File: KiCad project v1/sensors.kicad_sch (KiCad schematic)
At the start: 15 parts, among them Q1 TEMT6000X01, U6 BME280, U7 MAX4466EXK

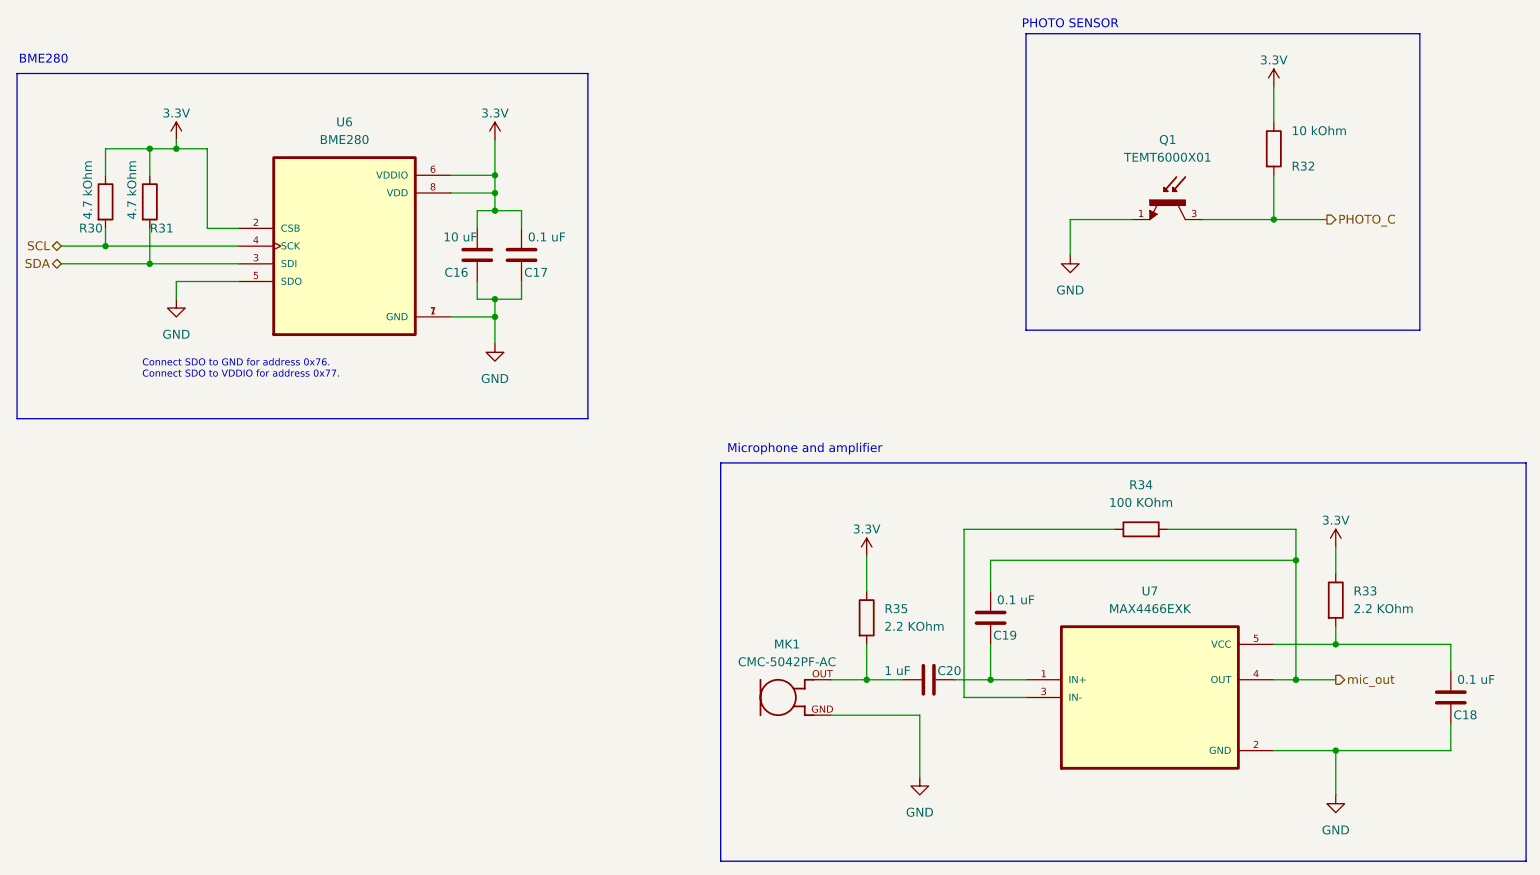
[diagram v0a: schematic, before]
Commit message: Added an OLED I2C display connector, boot and reset buttons, and breakout for remaining pins.
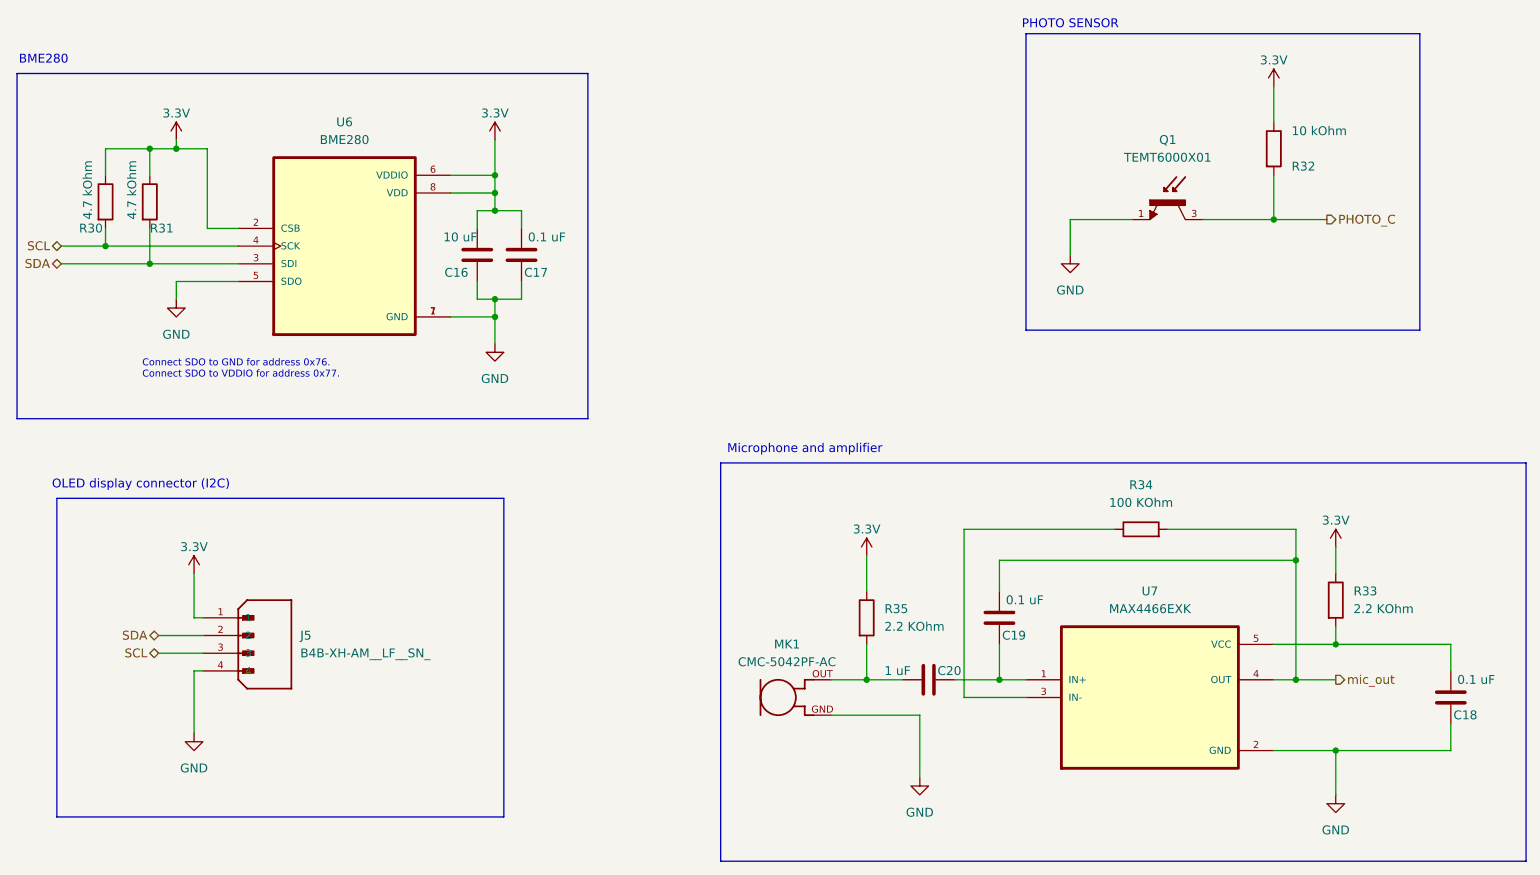
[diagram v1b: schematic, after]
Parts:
- added J5: B4B-XH-AM__LF__SN_, B4B-XH-AM__LF__SN_:JST_B4B-XH-AM__LF__SN_, symbol B4B-XH-AM__LF__SN_:B4B-XH-AM__LF__SN_
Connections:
- net 3.3V: now also J5.1
- net GND: now also J5.4
- net SCL: now also J5.3
- net SDA: now also J5.2
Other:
- note added: "OLED display connector (I2C)"
- moved on the sheet: C19

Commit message: Completed symbol and footprint associations.
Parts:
- R30, R31, R32, R33, R34, R35: footprint (none) -> Resistor_SMD:R_0201_0603Metric
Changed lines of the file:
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@@
 			)
 		)
-		(property "Footprint" ""
+		(property "Footprint" "Resistor_SMD:R_0201_0603Metric"
 			(at 182.88 97.028 90)
 			(effects
@@
 			)
 		)
-		(property "Footprint" ""
+		(property "Footprint" "Resistor_SMD:R_0201_0603Metric"
 			(at 209.042 105.41 90)
 			(effects
@@
 			)
 		)
-		(property "Footprint" ""
+		(property "Footprint" "Resistor_SMD:R_0201_0603Metric"
 			(at 141.732 107.95 90)
 			(effects
@@
 			)
 		)
-		(property "Footprint" ""
+		(property "Footprint" "Resistor_SMD:R_0201_0603Metric"
 			(at 32.512 48.26 90)
 			(effects
@@
 			)
 		)
-		(property "Footprint" ""
+		(property "Footprint" "Resistor_SMD:R_0201_0603Metric"
 			(at 38.862 48.26 90)
 			(effects
@@
 			)
 		)
-		(property "Footprint" ""
+		(property "Footprint" "Resistor_SMD:R_0201_0603Metric"
 			(at 200.152 40.64 90)
 			(effects

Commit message: Small fixes.
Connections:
- net mic_out renamed MIC_OUT
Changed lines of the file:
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@@
 	)
 	(junction
-		(at 205.105 116.84)
+		(at 205.74 116.84)
 		(diameter 0)
 		(color 0 0 0 0)
@@
 	)
 	(junction
+		(at 227.33 111.76)
+		(diameter 0)
+		(color 0 0 0 0)
+	)
+	(junction
 		(at 34.29 54.61)
 		(diameter 0)
@@
 	)
 	(junction
-		(at 205.105 99.695)
+		(at 205.74 100.33)
 		(diameter 0)
 		(color 0 0 0 0)
@@
 	(wire
 		(pts
-			(xy 205.105 99.695) (xy 205.105 116.84)
+			(xy 205.74 100.33) (xy 205.74 116.84)
 		)
 		(stroke
@@
 	(wire
 		(pts
-			(xy 205.105 116.84) (xy 210.82 116.84)
+			(xy 205.74 116.84) (xy 210.82 116.84)
 		)
 		(stroke
@@
 	(wire
 		(pts
-			(xy 201.93 116.84) (xy 205.105 116.84)
+			(xy 201.93 116.84) (xy 205.74 116.84)
 		)
 		(stroke
@@
 	(wire
 		(pts
-			(xy 186.69 95.25) (xy 205.105 95.25)
+			(xy 186.69 95.25) (xy 205.74 95.25)
 		)
 		(stroke
@@
 	(wire
 		(pts
+			(xy 227.33 105.41) (xy 227.33 111.76)
+		)
+		(stroke
+			(width 0)
+			(type default)
+		)
+	)
+	(wire
+		(pts
 			(xy 34.29 44.45) (xy 34.29 40.64)
 		)
@@
 	(wire
 		(pts
-			(xy 44.45 40.64) (xy 48.895 40.64)
+			(xy 44.45 40.64) (xy 49.53 40.64)
 		)
 		(stroke
@@
 	(wire
 		(pts
-			(xy 162.56 99.695) (xy 162.56 104.14)
+			(xy 162.56 100.33) (xy 162.56 104.14)
 		)
 		(stroke
@@
 	(wire
 		(pts
-			(xy 205.105 95.25) (xy 205.105 99.695)
+			(xy 205.74 95.25) (xy 205.74 100.33)
 		)
 		(stroke
@@
 	(wire
 		(pts
-			(xy 53.34 52.07) (xy 48.895 52.07)
-		)
-		(stroke
-			(width 0)
-			(type default)
-		)
-	)
-	(wire
-		(pts
-			(xy 48.895 52.07) (xy 48.895 40.64)
+			(xy 53.34 52.07) (xy 49.53 52.07)
+		)
+		(stroke
+			(width 0)
+			(type default)
+		)
+	)
+	(wire
+		(pts
+			(xy 49.53 52.07) (xy 49.53 40.64)
 		)
 		(stroke
@@
 	(wire
 		(pts
-			(xy 162.56 99.695) (xy 205.105 99.695)
+			(xy 162.56 100.33) (xy 205.74 100.33)
 		)
 		(stroke
@@
 		)
 	)
-	(hierarchical_label "mic_out"
+	(hierarchical_label "MIC_OUT"
 		(shape output)
 		(at 210.82 116.84 0)
@@
 					(unit 1)
 				)
+			)
+		)
+	)
+	(symbol
+		(lib_id "power:PWR_FLAG")
+		(at 227.33 105.41 0)
+		(unit 1)
+		(exclude_from_sim no)
+		(in_bom yes)
+		(on_board yes)
+		(dnp no)
+		(fields_autoplaced yes)
+		(property "Reference" "#FLG03"
+			(at 227.33 103.505 0)
+			(effects
+				(font
+					(size 1.27 1.27)
+				)
+				(hide yes)
+			)
+		)
+		(property "Value" "PWR_FLAG"
+			(at 227.33 100.33 0)
+			(effects
+				(font
+					(size 1.27 1.27)
+				)
+			)
+		)
+		(property "Footprint" ""
+			(at 227.33 105.41 0)
+			(effects
+				(font
+					(size 1.27 1.27)
+				)
+				(hide yes)
+			)
+		)
+		(property "Datasheet" "~"
+			(at 227.33 105.41 0)
+			(effects
+				(font
+					(size 1.27 1.27)
+				)
+				(hide yes)
+			)
+		)
+		(property "Description" "Special symbol for telling ERC where power comes from"
+			(at 227.33 105.41 0)
+			(effects
+				(font
+					(size 1.27 1.27)
+				)
+				(hide yes)
+			)
+		)
+		(pin "1"
+		)
+		(instances
+			(project ""
+				(path "/16c571a0-8550-4f05-972c-22b0701cbf02/09ec4a32-ddff-43cd-8e21-9ef822101853/23dfbcac-c55b-465d-b248-a44c230046f1"
+					(reference "#FLG03")
+					(unit 1)
+				)

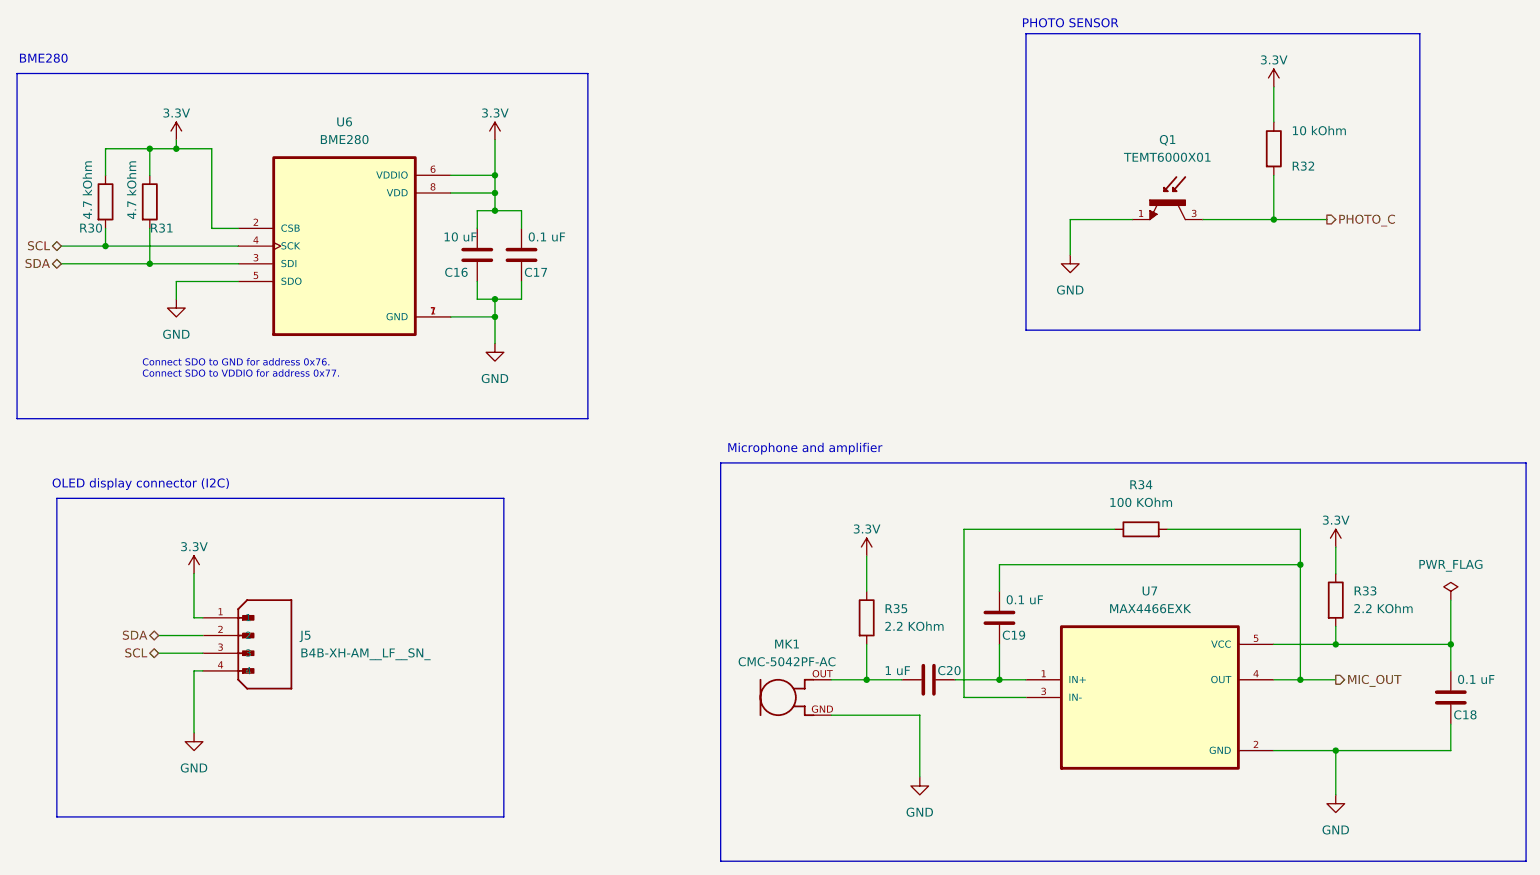
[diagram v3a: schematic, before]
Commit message: Simplifying component values by removing units.
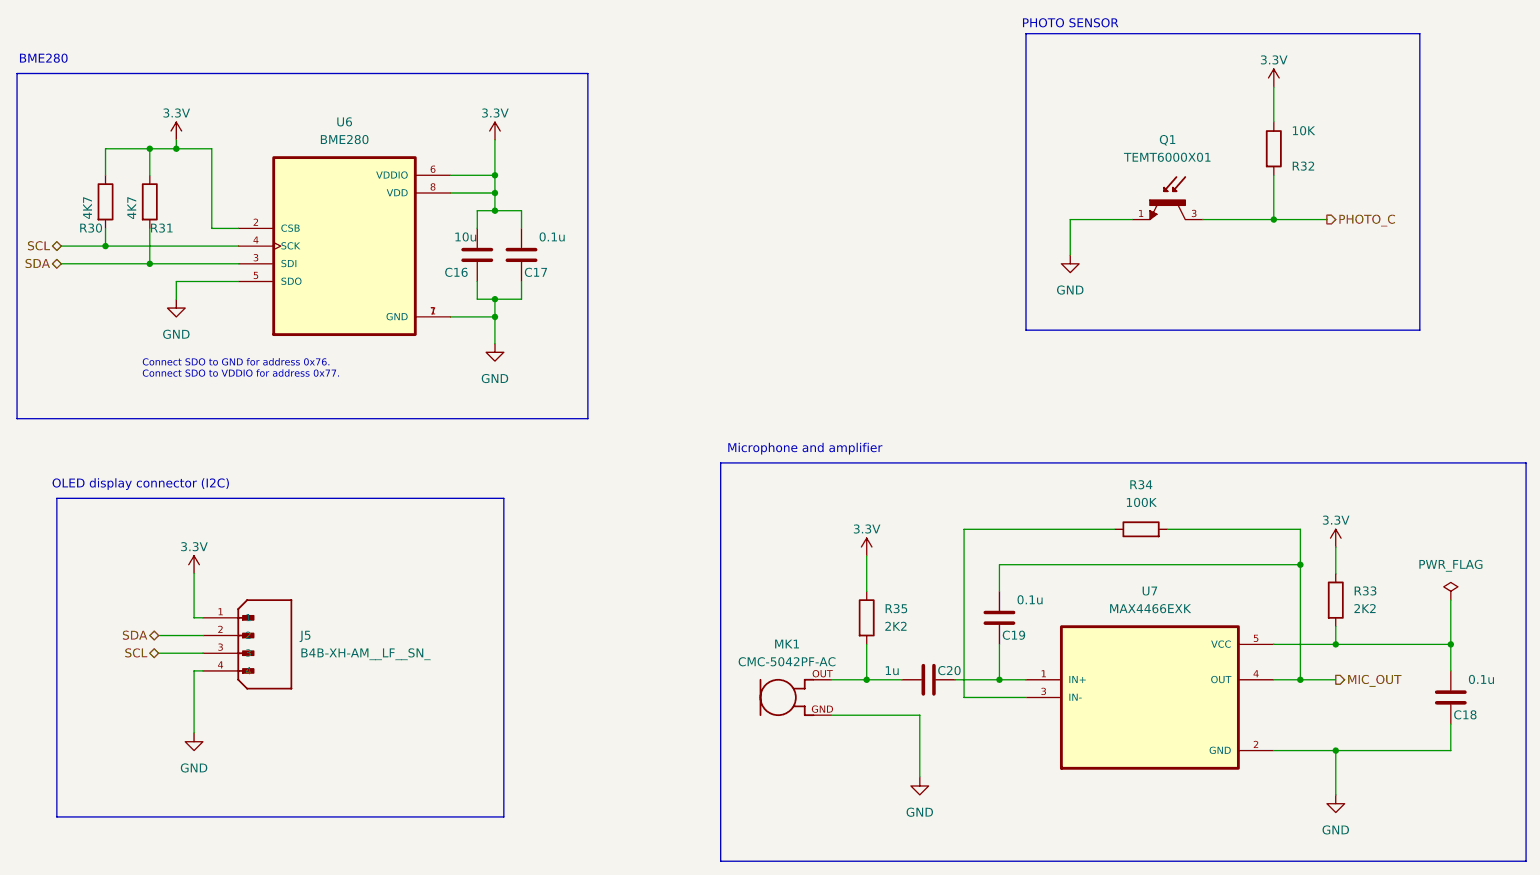
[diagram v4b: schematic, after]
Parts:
- C16: value 10 uF -> 10u
- C17, C18, C19: value 0.1 uF -> 0.1u
- C20: value 1 uF -> 1u
- R30, R31: value 4.7 kOhm -> 4K7
- R32: value 10 kOhm -> 10K
- R33, R35: value 2.2 KOhm -> 2K2
- R34: value 100 KOhm -> 100K
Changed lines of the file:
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@@
 			)
 		)
-		(property "Value" "100 KOhm"
+		(property "Value" "100K"
 			(at 182.88 91.44 90)
 			(effects
@@
 			)
 		)
-		(property "Value" "2.2 KOhm"
+		(property "Value" "2K2"
 			(at 213.36 106.6799 0)
 			(effects
@@
 			)
 		)
-		(property "Value" "2.2 KOhm"
+		(property "Value" "2K2"
 			(at 146.05 109.2199 0)
 			(effects
@@
 			)
 		)
-		(property "Value" "4.7 kOhm"
+		(property "Value" "4K7"
 			(at 31.75 50.8 90)
 			(effects
@@
 			)
 		)
-		(property "Value" "0.1 uF"
+		(property "Value" "0.1u"
 			(at 100.33 53.34 0)
 			(effects
@@
 			)
 		)
-		(property "Value" "4.7 kOhm"
+		(property "Value" "4K7"
 			(at 38.1 50.8 90)
 			(effects
@@
 			)
 		)
-		(property "Value" "0.1 uF"
+		(property "Value" "0.1u"
 			(at 168.91 105.41 0)
 			(effects
@@
 			)
 		)
-		(property "Value" "10 uF"
+		(property "Value" "10u"
 			(at 87.63 53.34 0)
 			(effects
@@
 			)
 		)
-		(property "Value" "0.1 uF"
+		(property "Value" "0.1u"
 			(at 233.68 116.84 0)
 			(effects
@@
 			)
 		)
-		(property "Value" "1 uF"
+		(property "Value" "1u"
 			(at 146.05 115.57 90)
 			(effects
@@
 			)
 		)
-		(property "Value" "10 kOhm"
+		(property "Value" "10K"
 			(at 204.47 38.1 0)
 			(effects
